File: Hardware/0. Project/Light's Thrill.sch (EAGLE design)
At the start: 0 parts

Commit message: Schematic 1.0 - DONE
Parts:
- added C1: 100uF x 16V, rcl:CPOL-EUE2-5
- added C2, C4, C5, C7: 1uF x 50V, rcl:C-EUC0805
- added C3, C6, C8: 100nF x 50V, rcl:C-EUC0805
- added CN1: USB-B Micro, USB Connectors:MICRO-USB
- added CN2: 2.1MMJACKTHM, adafruit:2.1MMJACKTHM
- added D1: US1A, diode:CGRM4007-G
- added LED1: RGB_LED_STRIP, led:RGB_LED_STRIP
- added Q1, Q2, Q3: SI2302DS, SI2302DS:SI2302DS
- added R1, R2, R3: 1k (5%), rcl:R-EU_M0805
- added R4, R8: 10k (5%), rcl:R-EU_M0805
- added R5: 100R (5%), rcl:R-EU_M0805
- added R6, R7: 22R (5%), rcl:R-EU_M0805
- added U$1: TSOP1838, TSOP1838:TSOP1838
- added U1: ATMEGA32U4, adafruit:ATMEGA32U4-AU
- added Y1: 16 MHz, crystal-geyer_V1_0:KX-9A
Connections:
- new net +12V: C8.1, CN2.TIP, D1.C, LED1G$4.ANODE
- new net +5V: C6.1, C7.1, CN1.VBUS, R4.2, R5.2, R8.2, U1.AVCC, U1.AVCC1, U1.UVCC, U1.VBUS, U1.VCC, U1.VCC1
- new net GND: C1.-, C2.2, C3.2, C4.2, C5.2, C6.2, C7.2, C8.2, CN1.GND, CN1.S, CN2.RING, CN2.RING_SW, D1.A, Q1.S, Q2.S, Q3.S, U$1.GND, U1.GND, U1.GND1, U1.GND2, U1.GND3, U1.PE2(!HWB), U1.UGND
- new net IR_SENSOR_SIGNAL: R4.1, U$1.OUT, U1.PE6(INT.6/AIN0)
- new net MCU_PWM_BLUE: R3.1, U1.PB6(OC1B/OC4B/ADC13)
- new net MCU_PWM_GREEN: R2.1, U1.PD7(OC4D/ADC10/T0)
- new net MCU_PWM_RED: R1.1, U1.PC6(OC3A/!OC4A)
- new net N$1: Q1.G, R1.2
- new net N$10: R8.1, U1./RESET
- new net N$11: C2.1, U1.UCAP
- new net N$12: C3.1, U1.AREF
- new net N$13: C4.1, U1.XTAL1, Y1.1
- new net N$14: C5.1, U1.XTAL2, Y1.2
- new net N$2: LED1-RED.C, Q1.D
- new net N$3: Q2.G, R2.2
- new net N$4: Q3.G, R3.2
- new net N$5: LED1-GREEN.C, Q2.D
- new net N$6: LED1-BLUE.C, Q3.D
- new net N$7: C1.+, R5.1, U$1.V+
- new net N$8: CN1.D-, R6.2
- new net N$9: CN1.D+, R7.2
- new net USB_D+: R7.1, U1.D+
- new net USB_D-: R6.1, U1.D-
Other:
- note added: "BLUE"
- note added: "D10"
- note added: "D5"
- note added: "D6"
- note added: "D7"
- note added: "GREEN"
- note added: "RED"

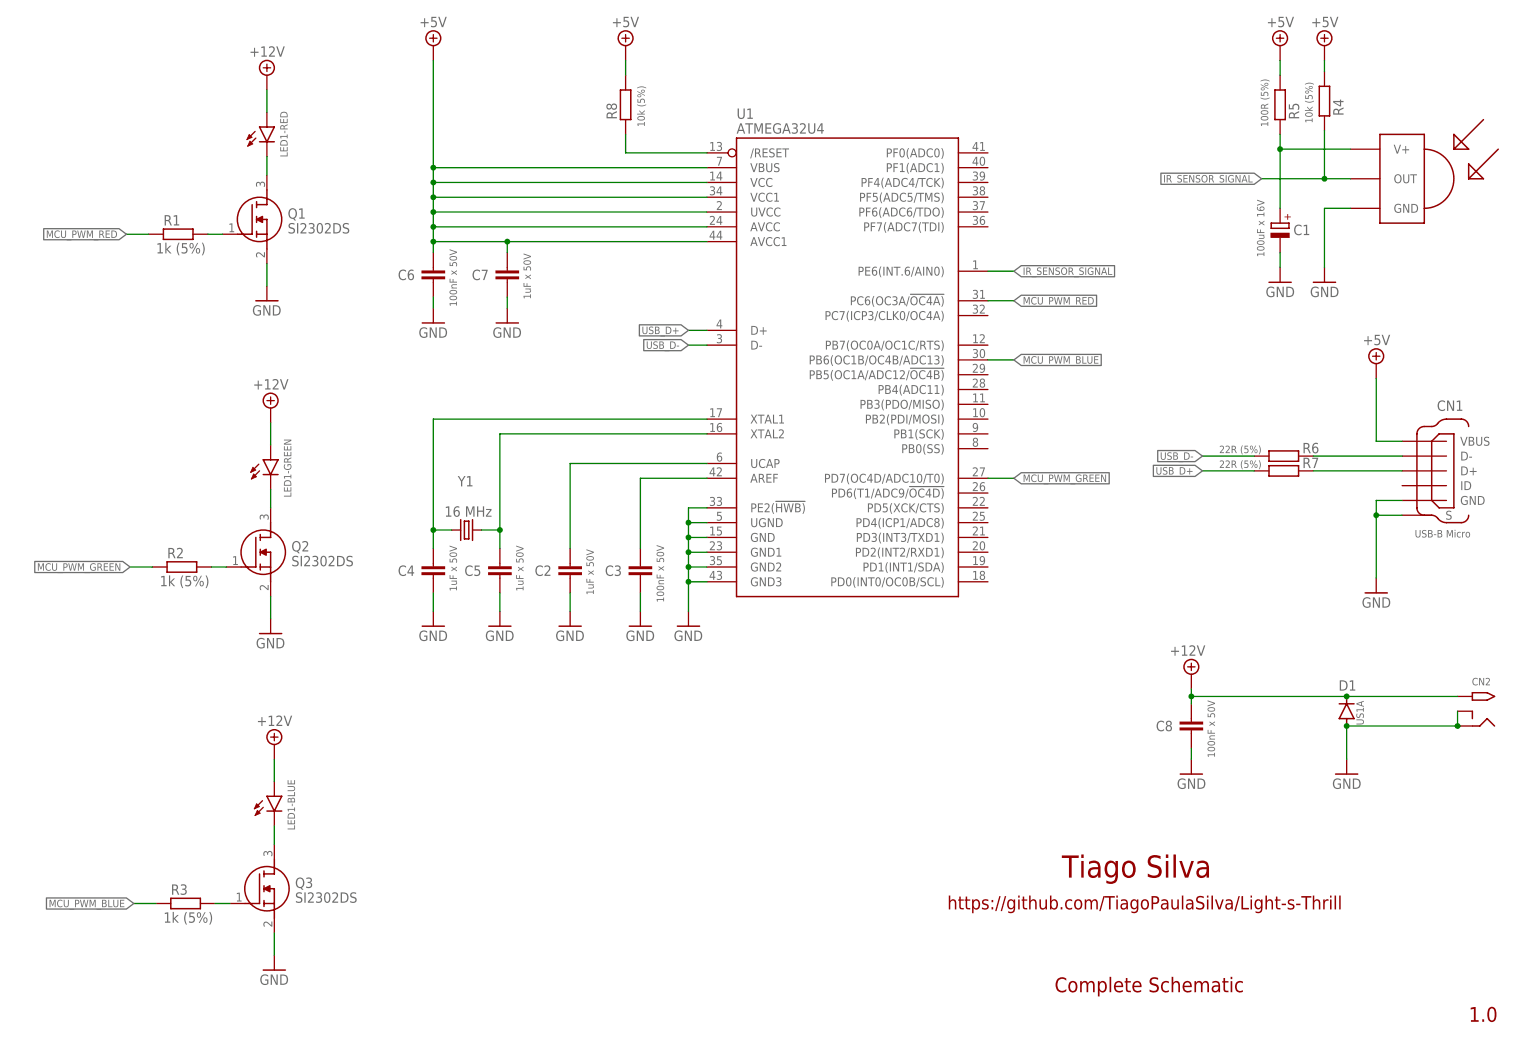
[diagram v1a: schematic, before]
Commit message: Schematic 1.1 - DONE
- User's interface circuit added (button and LED)
- 12V to 5V LDO added (working without a computer)
- External power supply circuit detect added
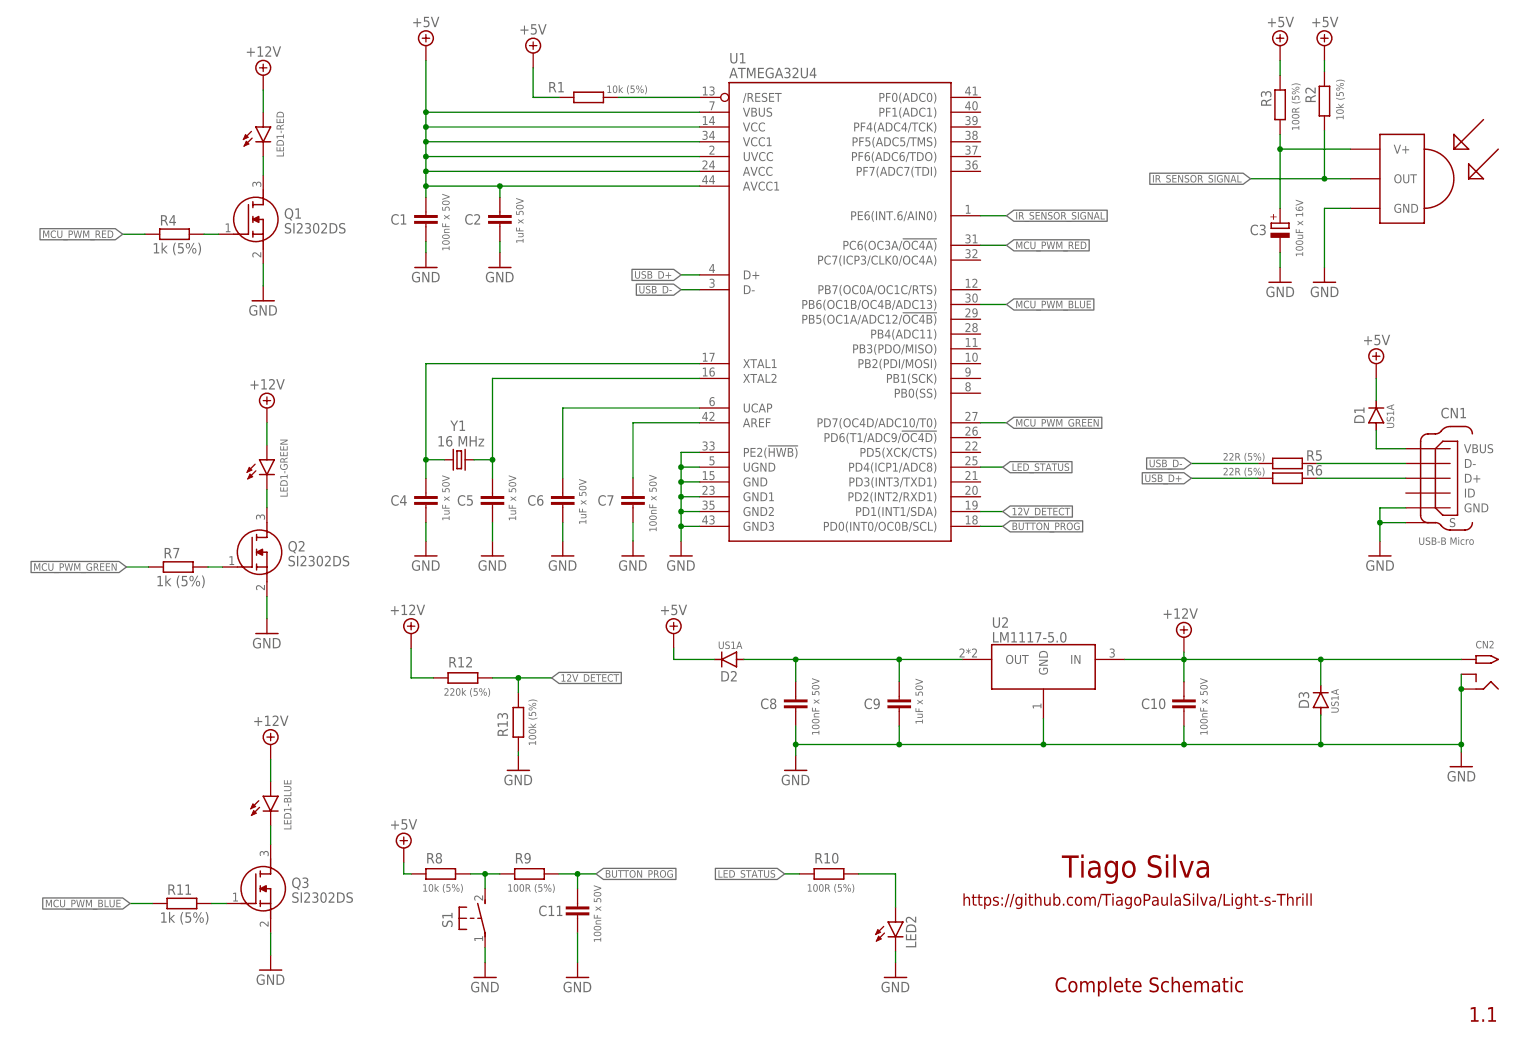
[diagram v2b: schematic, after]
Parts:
- added C10, C11: 100nF x 50V, rcl:C-EUC0805
- added C9: 1uF x 50V, rcl:C-EUC0805
- added D2, D3: US1A, diode:CGRM4007-G
- added LED2: (no value), led:LEDCHIPLED_0805
- added R10, R9: 100R (5%), rcl:R-EU_M0805
- added R11: 1k (5%), rcl:R-EU_M0805
- added R12: 220k (5%), rcl:R-EU_M0805
- added R13: 100k (5%), rcl:R-EU_M0805
- added S1: DTSM-3, switch-tact2:DTSM-3
- added U2: LM1117-5.0, LM1117IMP-5.0-NOPB:LM1117IMP-5.0-NOPB
- C1: value 100uF x 16V -> 100nF x 50V; device rcl:CPOL-EUE2-5 -> rcl:C-EUC0805
- C3: value 100nF x 50V -> 100uF x 16V; device rcl:C-EUC0805 -> rcl:CPOL-EUE2-5
- C6: value 100nF x 50V -> 1uF x 50V
- C7: value 1uF x 50V -> 100nF x 50V
- R1, R2: value 1k (5%) -> 10k (5%)
- R3: value 1k (5%) -> 100R (5%)
- R4: value 10k (5%) -> 1k (5%)
- R5: value 100R (5%) -> 22R (5%)
- R7: value 22R (5%) -> 1k (5%)
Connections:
- new net 12V_DETECT: R12.1, R13.2, U1.PD1(INT1/SDA)
- new net BUTTON_PROG: C11.1, R9.1, U1.PD0(INT0/OC0B/SCL)
- new net LED_STATUS: R10.1, U1.PD4(ICP1/ADC8)
- new net N$15: CN1.VBUS, D1.A
- new net N$16: C8.1, C9.1, D2.A, U2.OUT
- new net N$17: R8.2, R9.2, S1.2
- new net N$18: LED2.A, R10.2
- net +12V: now also C10.1, D3.C, R12.2, U2.IN; no longer C8.1, D1.C
- net +5V: now also C1.1, C2.1, D1.C, D2.C, R1.2, R2.1, R3.1, R8.1; no longer C6.1, C7.1, CN1.VBUS, R4.2, R5.2, R8.2
- net GND: now also C1.2, C10.2, C11.2, C3.-, C9.2, D3.A, LED2.C, R13.1, S1.1, U2.GND; no longer C1.-, C3.2, D1.A
- net IR_SENSOR_SIGNAL: now also R2.2; no longer R4.1
- net MCU_PWM_BLUE: now also R11.1; no longer R3.1
- net MCU_PWM_GREEN: now also R7.1; no longer R2.1
- net MCU_PWM_RED: now also R4.1; no longer R1.1
- net N$1: now also R4.2; no longer R1.2
- net N$10: now also R1.1; no longer R8.1
- net N$11: now also C6.1; no longer C2.1
- net N$12: now also C7.1; no longer C3.1
- net N$3: now also R7.2; no longer R2.2
- net N$4: now also R11.2; no longer R3.2
- net N$7: now also C3.+, R3.2; no longer C1.+, R5.1
- net N$8: now also R5.2; no longer R6.2
- net N$9: now also R6.2; no longer R7.2
- net USB_D+: now also R6.1; no longer R7.1
- net USB_D-: now also R5.1; no longer R6.1
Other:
- note added: "1.1"
- note added: "D2"
- note added: "D3"
- note added: "D4"
- note removed: "1.0"
- moved on the sheet: C2, C4, C5, C6, C7, C8, CN1, CN2, D1, LED1-BLUE, LED1-GREEN, LED1-RED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

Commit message: Schematic 1.2 - Minor improvements
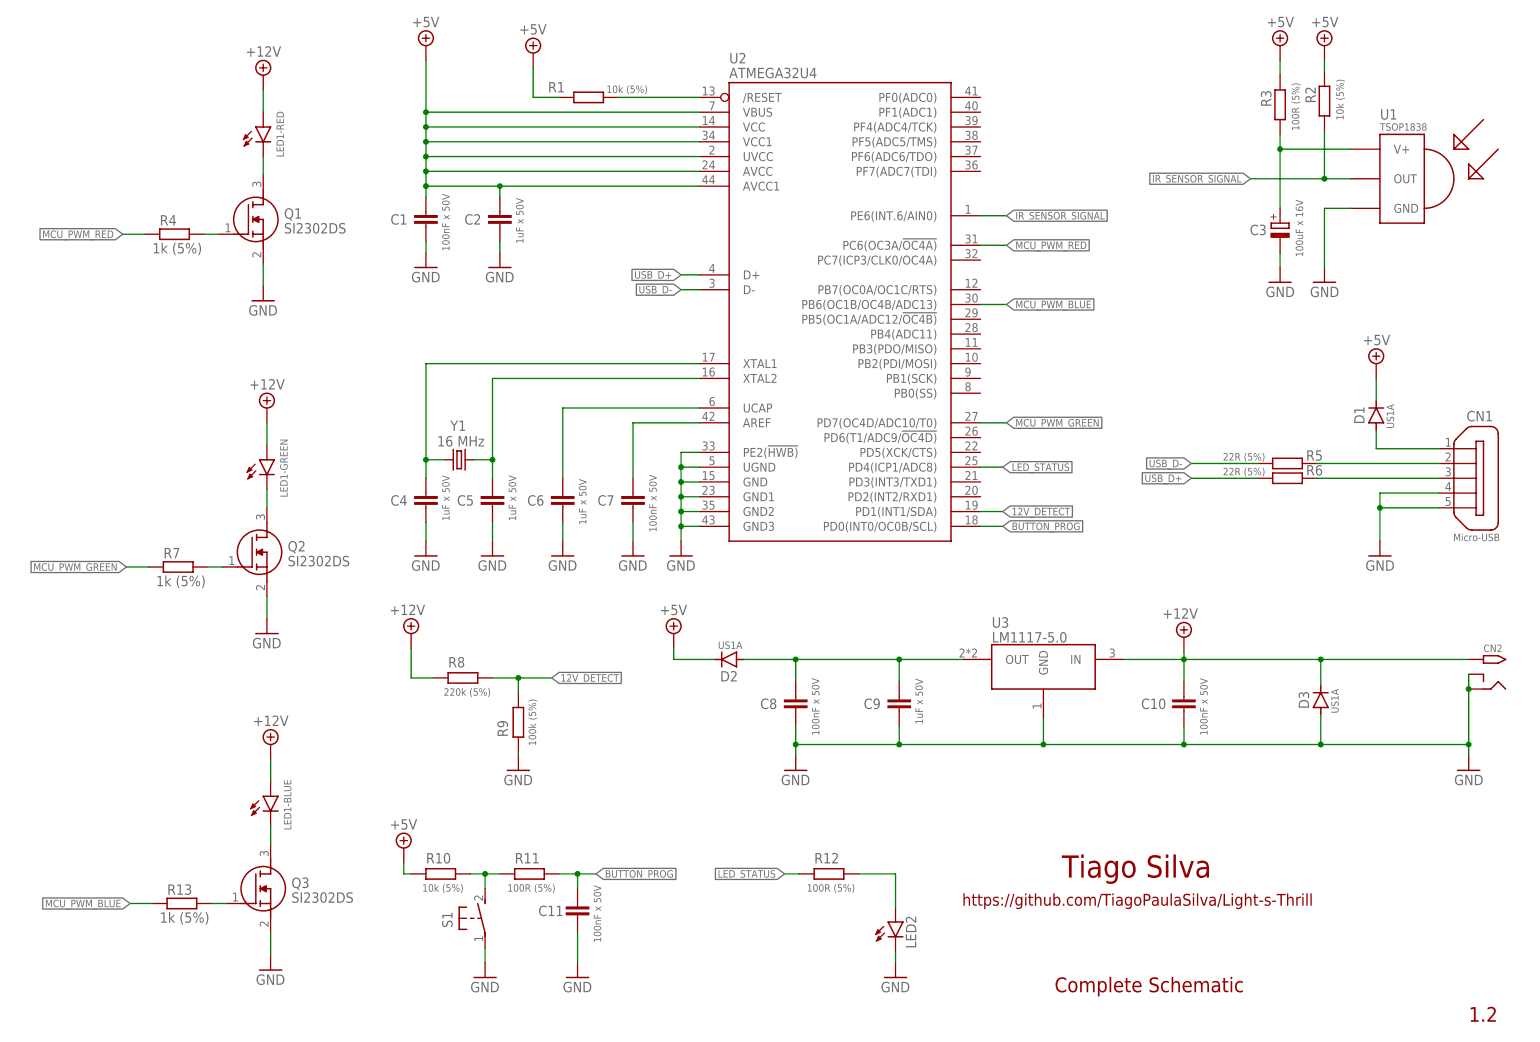
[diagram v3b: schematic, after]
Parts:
- removed U$1: TSOP1838, TSOP1838:TSOP1838
- added U3: LM1117-5.0, LM1117IMP-5.0-NOPB:LM1117IMP-5.0-NOPB
- CN1: value USB-B Micro -> Micro-USB; device USB Connectors:MICRO-USB -> Micro USB Connector:ZX62D-B-5PA8
- R10: value 100R (5%) -> 10k (5%)
- R11: value 1k (5%) -> 100R (5%)
- R12: value 220k (5%) -> 100R (5%)
- R13: value 100k (5%) -> 1k (5%)
- R8: value 10k (5%) -> 220k (5%)
- R9: value 100R (5%) -> 100k (5%)
- U1: value ATMEGA32U4 -> TSOP1838; device adafruit:ATMEGA32U4-AU -> TSOP1838:TSOP1838
- U2: value LM1117-5.0 -> ATMEGA32U4; device LM1117IMP-5.0-NOPB:LM1117IMP-5.0-NOPB -> adafruit:ATMEGA32U4-AU
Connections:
- net +12V: now also R8.2, U3.IN; no longer R12.2, U2.IN
- net +5V: now also R10.1, U2.AVCC, U2.AVCC1, U2.UVCC, U2.VBUS, U2.VCC, U2.VCC1; no longer R8.1, U1.AVCC, U1.AVCC1, U1.UVCC, U1.VBUS, U1.VCC, U1.VCC1
- net 12V_DETECT: now also R8.1, R9.2, U2.PD1(INT1/SDA); no longer R12.1, R13.2, U1.PD1(INT1/SDA)
- net BUTTON_PROG: now also R11.1, U2.PD0(INT0/OC0B/SCL); no longer R9.1, U1.PD0(INT0/OC0B/SCL)
- net GND: now also CN1G$1.4, CN1G$1.5, R9.1, U2.GND1, U2.GND2, U2.GND3, U2.PE2(!HWB), U2.UGND, U3.GND; no longer CN1.GND, CN1.S, R13.1, U$1.GND, U1.GND1, U1.GND2, U1.GND3, U1.PE2(!HWB), U1.UGND
- net IR_SENSOR_SIGNAL: now also U1.OUT, U2.PE6(INT.6/AIN0); no longer U$1.OUT, U1.PE6(INT.6/AIN0)
- net LED_STATUS: now also R12.1, U2.PD4(ICP1/ADC8); no longer R10.1, U1.PD4(ICP1/ADC8)
- net MCU_PWM_BLUE: now also R13.1, U2.PB6(OC1B/OC4B/ADC13); no longer R11.1, U1.PB6(OC1B/OC4B/ADC13)
- net MCU_PWM_GREEN: now also U2.PD7(OC4D/ADC10/T0); no longer U1.PD7(OC4D/ADC10/T0)
- net MCU_PWM_RED: now also U2.PC6(OC3A/!OC4A); no longer U1.PC6(OC3A/!OC4A)
- net N$10: now also U2./RESET; no longer U1./RESET
- net N$11: now also U2.UCAP; no longer U1.UCAP
- net N$12: now also U2.AREF; no longer U1.AREF
- net N$13: now also U2.XTAL1; no longer U1.XTAL1
- net N$14: now also U2.XTAL2; no longer U1.XTAL2
- net N$15: now also CN1G$1.1; no longer CN1.VBUS
- net N$16: now also U3.OUT; no longer U2.OUT
- net N$17: now also R10.2, R11.2; no longer R8.2, R9.2
- net N$18: now also R12.2; no longer R10.2
- net N$4: now also R13.2; no longer R11.2
- net N$7: now also U1.V+; no longer U$1.V+
- net N$8: now also CN1G$1.2; no longer CN1.D-
- net N$9: now also CN1G$1.3; no longer CN1.D+
- net USB_D+: now also U2.D+; no longer U1.D+
- net USB_D-: now also U2.D-; no longer U1.D-
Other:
- note added: "1.2"
- note removed: "1.1"
- moved on the sheet: CN2, R10, R11, R12, R13, R8, R9
